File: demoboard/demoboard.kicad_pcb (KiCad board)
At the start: 2 copper layers, 38.1 x 50.8 mm, 39 parts, among them CON1 BARREL_JACK, M1 ESP-07, P1 USB_OTG, P2 header1, Q1 BC547, Q2 BC547, SW1 UI1, SW2 UI1, U1 CH340G, U2 1117-5v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

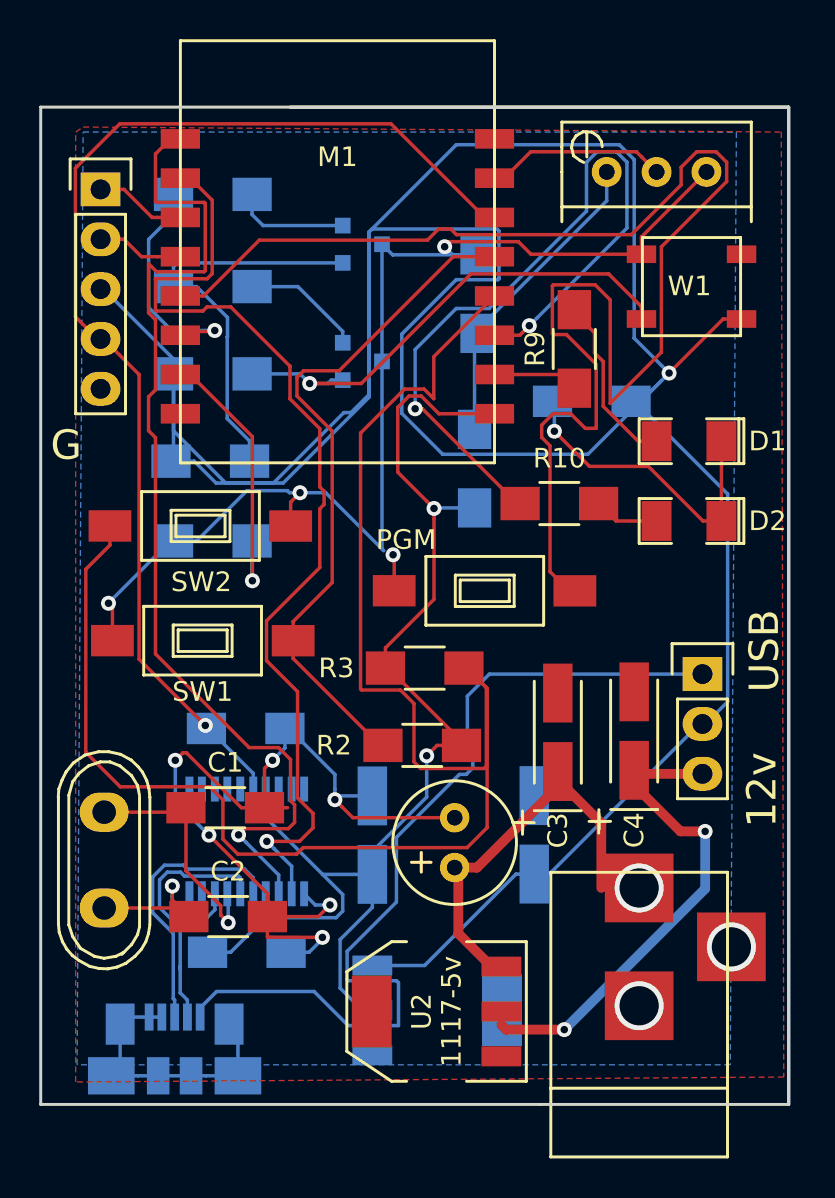
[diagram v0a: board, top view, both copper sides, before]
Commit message: lot f correction in routing and corrected solder mask clearence
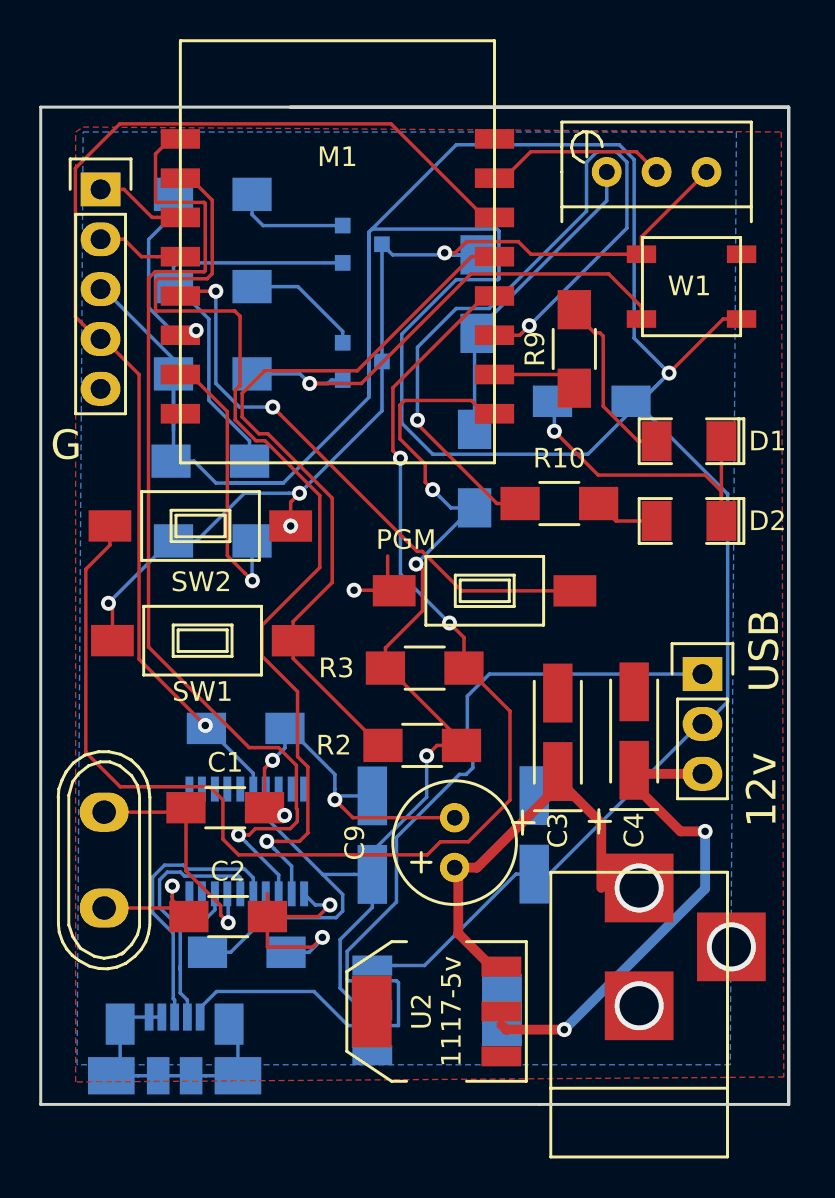
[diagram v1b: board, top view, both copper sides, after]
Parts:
- added REF**: Symbol_OSHW-Logo_SilkScreen, Symbols:Symbol_OSHW-Logo_SilkScreen, B.Cu at (153.8, 100.6)
- C9: footprint Capacitors_Elko_ThroughHole:Elko_vert_11.2x6.3mm_RM2.5 -> Capacitors_Elko_ThroughHole:Elko_vert_11.2x6.3mm_RM2.5_CopperClear
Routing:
- net Net-(M1-Pad5): track 76.4 -> 29.6 mm, vias 0 -> 2
- net GND: track 138.1 -> 119.7 mm
- net Net-(M1-Pad12): track 84.8 -> 68.8 mm, vias 0 -> 2
- net 5v: track 166.0 -> 156.4 mm
- net Net-(M1-Pad13): track 34.9 -> 38.6 mm
- net 3v3In: track 11.2 -> 9.29 mm
- net RX: track 52.8 -> 51.9 mm
- net Net-(Q1-Pad1): track 20.9 -> 20.3 mm
- net 3v3: track 125.6 -> 126.1 mm, vias 3 -> 4

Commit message: strengthened power lines. shortned traces
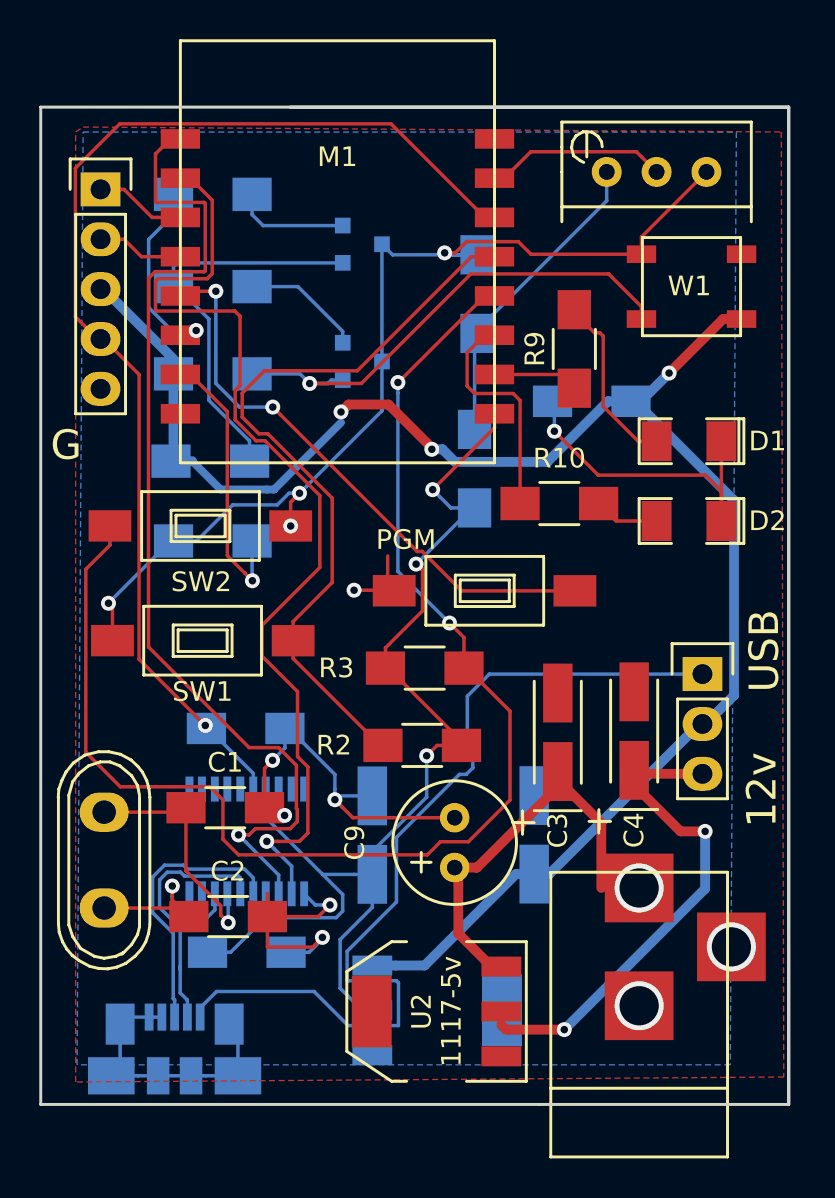
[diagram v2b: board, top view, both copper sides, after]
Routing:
- net 5v: track 156.4 -> 88.0 mm, vias 1 -> 3
- net Net-(M1-Pad11): track 39.6 -> 11.7 mm, vias 2 -> 0
- net 3v3: track 126.1 -> 121.6 mm
